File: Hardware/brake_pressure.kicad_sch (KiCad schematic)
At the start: 13 parts, among them U15 MCP6002-xMC

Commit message: Changes in power section
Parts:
- TP10, TP11, TP12, TP9: footprint TestPoint:TestPoint_Pad_D1.0mm -> TestPoint:TestPoint_THTPad_D1.0mm_Drill0.5mm
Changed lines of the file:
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@@
 			)
 		)
-		(property "Footprint" "TestPoint:TestPoint_Pad_D1.0mm"
+		(property "Footprint" "TestPoint:TestPoint_THTPad_D1.0mm_Drill0.5mm"
 			(at 161.29 93.345 0)
 			(effects
@@
 			)
 		)
-		(property "Footprint" "TestPoint:TestPoint_Pad_D1.0mm"
+		(property "Footprint" "TestPoint:TestPoint_THTPad_D1.0mm_Drill0.5mm"
 			(at 121.92 90.805 0)
 			(effects
@@
 			)
 		)
-		(property "Footprint" "TestPoint:TestPoint_Pad_D1.0mm"
+		(property "Footprint" "TestPoint:TestPoint_THTPad_D1.0mm_Drill0.5mm"
 			(at 132.08 95.885 0)
 			(effects
@@
 			)
 		)
-		(property "Footprint" "TestPoint:TestPoint_Pad_D1.0mm"
+		(property "Footprint" "TestPoint:TestPoint_THTPad_D1.0mm_Drill0.5mm"
 			(at 185.42 95.885 0)
 			(effects

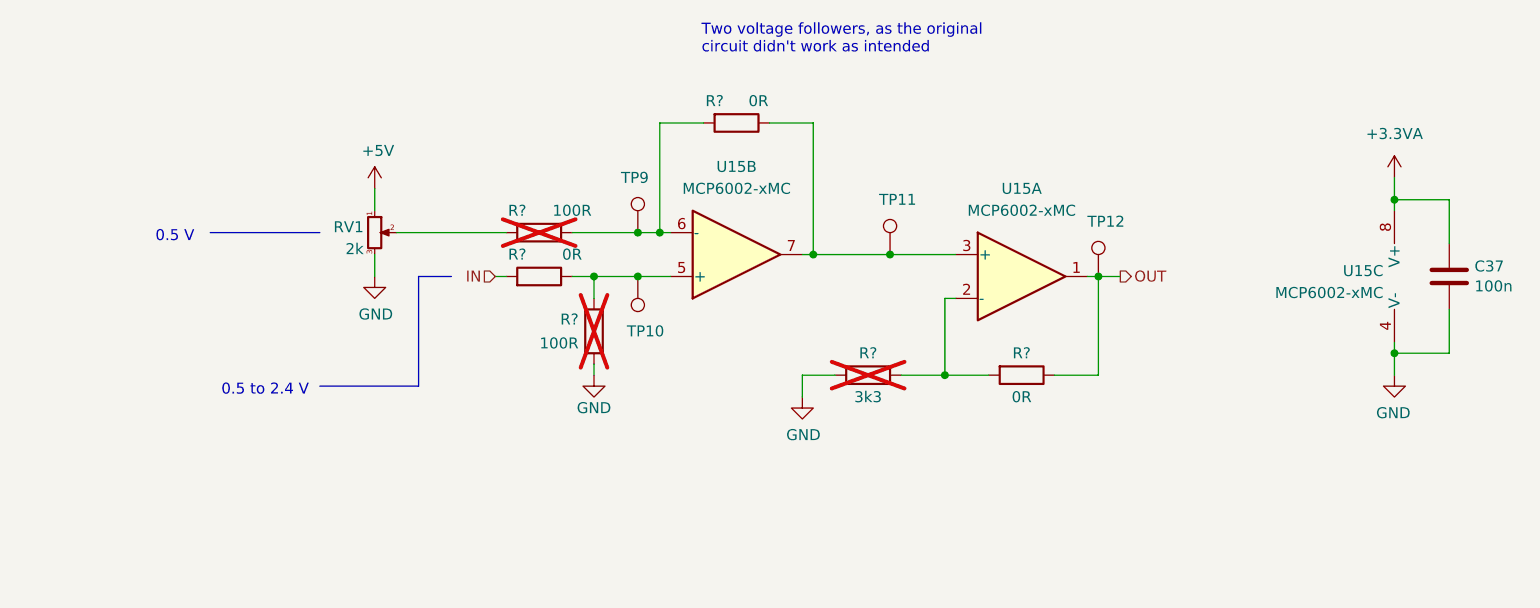
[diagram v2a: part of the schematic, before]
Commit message: Changes Vcc op-amps in brakes pressure (3V3 to 5V) and mcp6002 footprint (to MSOP8)
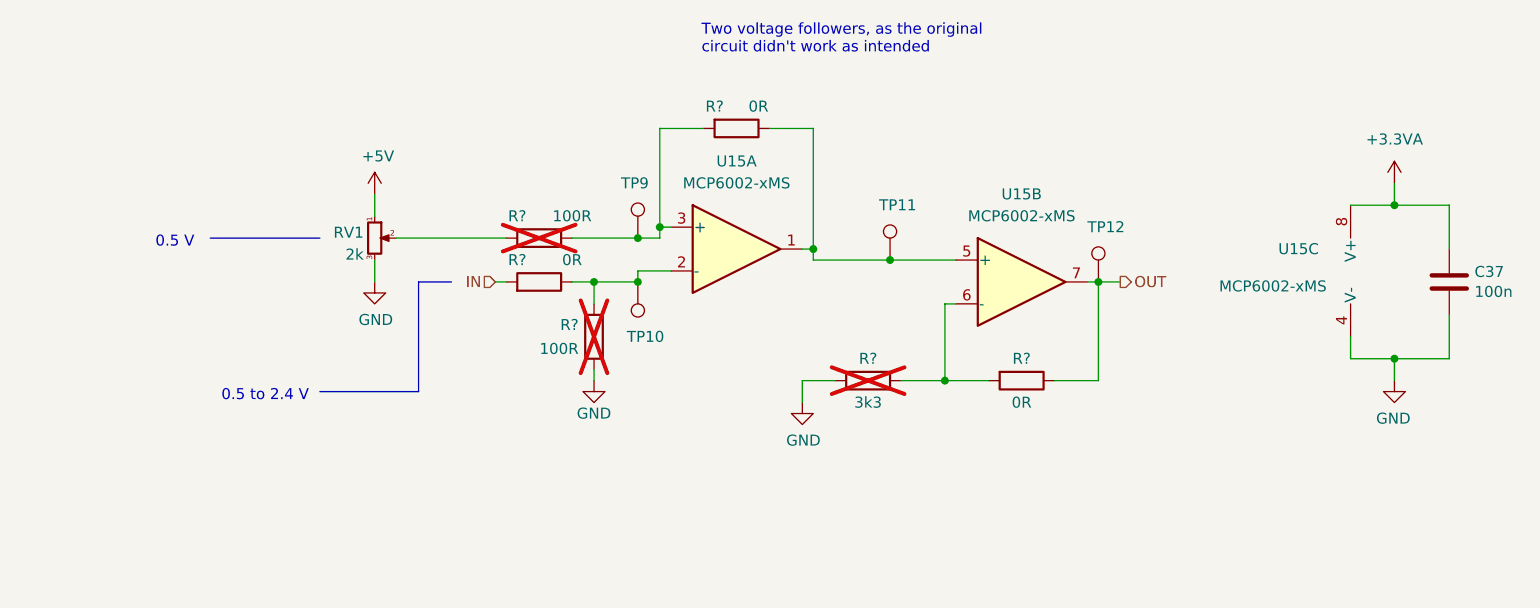
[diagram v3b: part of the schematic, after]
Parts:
- removed U15: MCP6002-xMC, Package_DFN_QFN:DFN-8-1EP_3x2mm_P0.5mm_EP1.7x1.4mm, symbol Amplifier_Operational:MCP6002-xMC
- added U15: MCP6002-xMS, Snapeda:SOP65P490X110-8N, symbol Amplifier_Operational:MCP6002-xMS
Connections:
- net +3.3VA: now also U15.8 (V+)
- net GND: now also U15.4 (V-)
- net OUT: now also U15.7
- net at R?.1, TP11.1: now also U15.1, U15.5 (+)
- net at R?.1, R?.2, TP10.1: now also U15.2 (-)
- net at R?.1, R?.2, TP9.1: now also U15.3 (+)
- net at R?.1, R?.2: now also U15.6 (-)
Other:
- moved on the sheet: C37, R?, RV1, TP10, TP11, TP12, TP9
